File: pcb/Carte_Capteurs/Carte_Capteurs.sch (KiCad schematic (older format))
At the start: 0 parts

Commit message: demarrage carte capteurs
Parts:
- added Logo1: LOGO, Insa:insa-image, symbol insa-sym:LOGO
- added U1: FRDM-KL25Z, Insa:FRDM-KL25Z, symbol Insa:FRDM-KL25Z
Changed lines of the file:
@@
 EESchema Schematic File Version 4
+LIBS:Carte_Capteurs-cache
 EELAYER 26 0
 EELAYER END
@@
 Comment4 ""
 $EndDescr
+$Comp
+L Insa:FRDM-KL25Z U1
+U 1 1 5DFFCA8E
+P 3150 6900
+F 0 "U1" H 3150 9098 50  0000 C CNN
+F 1 "FRDM-KL25Z" H 3150 9007 50  0000 C CNN
+F 2 "Insa:FRDM-KL25Z" H 3100 6250 50  0001 C CNN
+F 3 "" H 3100 6250 50  0001 C CNN
+	1    3150 6900
+	1    0    0    -1
+$EndComp
+$Comp
+L insa-sym:LOGO Logo1
+U 1 1 5DFFCBC5
+P 7550 6800
+F 0 "Logo1" H 7550 6348 60  0001 C CNN
+F 1 "LOGO" H 7550 7252 60  0001 C CNN
+F 2 "Insa:insa-image" H 7550 6800 50  0001 C CNN
+F 3 "" H 7550 6800 50  0001 C CNN
+	1    7550 6800
+	1    0    0    -1
+$EndComp
 $EndSCHEMATC

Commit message: version d'echange
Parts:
- added C1, C4: 100nF, Capacitor_SMD:C_1206_3216Metric_Pad1.42x1.75mm_HandSolder, symbol Device:C
- added C2, C3: 100µF, Capacitor_THT:CP_Radial_D6.3mm_P2.50mm, symbol Device:CP
- added D1: LED, LED_THT:LED_D3.0mm, symbol Device:LED
- added J10, J9: Conn_01x05, Connector_PinHeader_2.54mm:PinHeader_1x05_P2.54mm_Horizontal, symbol Connector_Generic:Conn_01x05
- added J11, J12: Conn_01x04, Connector_PinHeader_2.54mm:PinHeader_1x04_P2.54mm_Horizontal, symbol Connector_Generic:Conn_01x04
- added J5: Conn_02x07_Odd_Even, Connector_PinHeader_2.54mm:PinHeader_2x07_P2.54mm_Vertical, symbol Connector_Generic:Conn_02x07_Odd_Even
- added J6: Molex KK 254, Connector_Molex:Molex_KK-254_AE-6410-04A_1x04_P2.54mm_Vertical, symbol Connector_Generic:Conn_01x04
- added J7, J8: Samtec FTS-105-01-L-DV, Connector_PinHeader_1.27mm:PinHeader_2x05_P1.27mm_Vertical, symbol Connector_Generic:Conn_02x05_Odd_Even
- added R1: R, Resistor_SMD:R_1206_3216Metric_Pad1.42x1.75mm_HandSolder, symbol Device:R
- added U2: XBee, Insa:Xbee3, symbol Insa:XBee
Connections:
- net +BATT: now reaches U1.3.16 (VIN)
- net +BATT: now also C3.1, C4.1, J6.1 (Pin_1)
- net PWR_LED: now reaches U1.3.4 (3V3)
- net PWR_LED: now also D1.2 (A)
- new net: D1.1 (K), R1.1
- new net +3V3: C1.1, C2.1, J6.3 (Pin_3), U2.1 (VCC)
- new net DISABLE_MOT_R: J5.1 (Pin_1)
- new net DISBALE_MOT_L: J5.3 (Pin_3)
- new net FEEDBACK_MOT_L: J5.6 (Pin_6)
- new net FEEDBACK_MOT_R: J5.4 (Pin_4)
- new net GND: C1.2, C2.2, C3.2, C4.2, J5.11 (Pin_11), J5.13 (Pin_13), J5.5 (Pin_5), J5.7 (Pin_7), J5.9 (Pin_9), J6.2 (Pin_2), J6.4 (Pin_4), R1.2, U2.10 (GND)
- new net PWM_MOT_L_1: J5.12 (Pin_12)
- new net PWM_MOT_L_2: J5.14 (Pin_14)
- new net PWM_MOT_R_1: J5.8 (Pin_8)
- new net PWM_MOT_R_2: J5.10 (Pin_10)
- new net SERVO_PWM: J5.2 (Pin_2)
- new net USART_RX: U2.2 (DOUT)
- new net USART_TX: U2.3 (DIN)

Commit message: sauvegarde intermediaire
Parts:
- added C10, C11, C5, C6, C7, C8, C9: 100nF, Capacitor_SMD:C_1206_3216Metric_Pad1.42x1.75mm_HandSolder, symbol Device:C
- added J13: Conn_01x02, Connector_PinHeader_2.54mm:PinHeader_1x02_P2.54mm_Vertical, symbol Connector_Generic:Conn_01x02
- added Q1: NTR3C21NZT1G, Package_TO_SOT_SMD:SOT-23, symbol Device:Q_NMOS_GSD
- added R3, R4: 10K, Resistor_SMD:R_1206_3216Metric_Pad1.42x1.75mm_HandSolder, symbol Device:R
- added R5: 100R, Resistor_SMD:R_1206_3216Metric_Pad1.42x1.75mm_HandSolder, symbol Device:R
- added RN1, RN2: 100R, Resistor_SMD:R_Array_Convex_4x1206, symbol Device:R_Pack04
- added RN3: 10K, Resistor_SMD:R_Array_Convex_4x1206, symbol Device:R_Pack04
- added SW1: SMR8016C-1, Insa:Nidec_Copal_SMR-8016C, symbol Switch:SW_Coded_SH-7050
- added SW2: Reset, Button_Switch_THT:SW_PUSH_6mm_H4.3mm, symbol Switch:SW_Push
- added SW3: USER1, Button_Switch_THT:SW_PUSH_6mm_H4.3mm, symbol Switch:SW_Push
- added SW4: USER2, Button_Switch_THT:SW_PUSH_6mm_H4.3mm, symbol Switch:SW_Push
- added U3: HDSP-7501, Display_7Segment:HDSP-A151, symbol Display_Character:HDSP-7501
- added U4: TCL6C598, Package_SO:TSSOP-16_4.4x5mm_P0.65mm, symbol Insa:TCL6C598
- J10, J9: value Conn_01x05 -> DF3A-5P-2DS; footprint Connector_PinHeader_2.54mm:PinHeader_1x05_P2.54mm_Horizontal -> Insa:DF3A-5P-2DS
- J11, J12: value Conn_01x04 -> DF3A-4P-2DS; footprint Connector_PinHeader_2.54mm:PinHeader_1x04_P2.54mm_Horizontal -> Insa:DF3A-4P-2DS
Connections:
- net DISBALE_MOT_L is gone; now on net DISABLE_MOT_L: J5.3 (Pin_3)
- net +3V3: now also J10.2 (Pin_2), J11.1 (Pin_1), J12.1 (Pin_1), J7.8 (Pin_8), J8.8 (Pin_8), J9.2 (Pin_2), C10.1, C11.1, C5.1, C6.1, C7.1, C8.1, C9.1, R3.1, R4.1, SW1.C, U3.1 (CA), U3.6 (CA), U4.1 (VCC), U4.7 (~CLR)
- net +BATT: now also J13.1 (Pin_1)
- net DISABLE_MOT_R: now also U1.1.1 (PTC7)
- net FEEDBACK_MOT_L: now also U1.2.17 (PTD6)
- net FEEDBACK_MOT_R: now also U1.2.4 (PTD5)
- net GND: now also J10.5 (Pin_5), J11.3 (Pin_3), J12.3 (Pin_3), J7.1 (Pin_1), J7.10 (Pin_10), J7.3 (Pin_3), J7.5 (Pin_5), J7.7 (Pin_7), J7.9 (Pin_9), J8.1 (Pin_1), J8.10 (Pin_10), J8.3 (Pin_3), J8.5 (Pin_5), J8.7 (Pin_7), J8.9 (Pin_9), J9.5 (Pin_5), U1.2.14 (GND), U1.3.12 (GND), U1.3.14 (GND), C10.2, C11.2, C5.2, C6.2, C7.2, C8.2, C9.2, Q1.2 (S), RN3.1 (R1.1), RN3.2 (R2.1), RN3.3 (R3.1), RN3.4 (R4.1), SW2.1, SW3.1, SW4.1, U4.16 (GND), U4.8 (~G)
- net PWM_MOT_L_1: now also U1.1.14 (PTC8)
- net PWM_MOT_L_2: now also U1.1.16 (PTC9)
- net PWM_MOT_R_1: now also U1.1.10 (PTA4)
- net PWM_MOT_R_2: now also U1.1.12 (PTA5)
- net SERVO_PWM: now also U1.1.8 (PTA12)
- net USART_RX: now also U1.4.7 (PTE23)
- net USART_TX: now also U1.4.5 (PTE22)
- net DISP_SIN: now reaches U1.1.11 (PTC6)
- net DISP_SIN: now also U4.2 (SIN)
- net DISP_LATCH: now reaches U1.1.13 (PTC10)
- net DISP_LATCH: now also U4.10 (RCK)
- net ENC_SIG_B1: now reaches U1.1.2 (PTA1)
- net ENC_SIG_B1: now also J9.4 (Pin_4)
- net DISABLE_MOT_L: now reaches U1.1.3 (PTC0)
- net ENC_SIG_B2: now reaches U1.1.4 (PTA2)
- net ENC_SIG_B2: now also J10.4 (Pin_4)
- net ENC_INDEX1: now reaches U1.1.6 (PTD4)
- net ENC_INDEX1: now also J9.1 (Pin_1)
- net DISP_CLK: now reaches U1.1.9 (PTC5)
- net DISP_CLK: now also U4.15 (SRCK)
- net CAM_LED: now reaches U1.2.1 (PTC12)
- net CAM_LED: now also R5.1
- net SW_USER1: now reaches U1.2.10 (PTD3)
- net SW_USER1: now also R3.2, SW3.2
- net SW_USER2: now reaches U1.2.12 (PTD1)
- net SW_USER2: now also R4.2, SW4.2
- net SENS_SCL1: now reaches U1.2.18 (PTE1)
- net SENS_SCL1: now also J11.4 (Pin_4)
- net ENC_INDEX2: now reaches U1.2.2 (PTA13)
- net ENC_INDEX2: now also J10.1 (Pin_1)
- net SENS_SDA1: now reaches U1.2.20 (PTE0)
- net SENS_SDA1: now also J11.2 (Pin_2)
- net CCD_SI0: now reaches U1.3.1 (PTB8)
- net CCD_SI0: now also J7.4 (Pin_4)
- net ROT_SW_2: now reaches U1.3.11 (PTE3)
- net ROT_SW_2: now also RN3.7 (R2.2), SW1.2
- net ROT_SW_4: now reaches U1.3.13 (PTE4)
- net ROT_SW_4: now also RN3.6 (R3.2), SW1.4
- net ROT_SW_8: now reaches U1.3.15 (PTE5)
- net ROT_SW_8: now also RN3.5 (R4.2), SW1.8
- net CCD_CLK0: now reaches U1.3.3 (PTB9)
- net CCD_CLK0: now also J7.6 (Pin_6)
- net CCD_SI1: now reaches U1.3.5 (PTB10)
- net CCD_SI1: now also J8.4 (Pin_4)
- net RESET: now reaches U1.3.6 (PTA20)
- net RESET: now also SW2.2
- net CCD_CLK1: now reaches U1.3.7 (PTB11)
- net CCD_CLK1: now also J8.6 (Pin_6)
- net ROT_SW_1: now reaches U1.3.9 (PTE2)
- net ROT_SW_1: now also RN3.8 (R1.2), SW1.1
- net CCD_AD0: now reaches U1.4.10 (PTC2)
- net CCD_AD0: now also J7.2 (Pin_2)
- net CCD_AD1: now reaches U1.4.12 (PTC1)
- net CCD_AD1: now also J8.2 (Pin_2)
- net SENS_SCL2: now reaches U1.4.2 (PTB0)
- net SENS_SCL2: now also J12.4 (Pin_4)
- net SENS_SDA2: now reaches U1.4.4 (PTB1)
- net SENS_SDA2: now also J12.2 (Pin_2)
- net ENC_SIG_A1: now reaches U1.4.6 (PTB2)
- net ENC_SIG_A1: now also J9.3 (Pin_3)
- net ENC_SIG_A2: now reaches U1.4.8 (PTB3)
- net ENC_SIG_A2: now also J10.3 (Pin_3)
- new net: RN1.4 (R4.1), U3.10 (A)
- new net: RN2.3 (R3.1), U3.2 (F)
- new net: RN2.2 (R2.1), U3.3 (G)
- new net: RN2.4 (R4.1), U3.4 (E)
- new net: RN1.1 (R1.1), U3.5 (D)
- new net: RN2.1 (R1.1), U3.7 (DP)
- new net: RN1.2 (R2.1), U3.8 (C)
- new net: RN1.3 (R3.1), U3.9 (B)
- new net: RN2.5 (R4.2), U4.11 (DRAIN4)
- new net: RN2.6 (R3.2), U4.12 (DRAIN5)
- new net: RN2.7 (R2.2), U4.13 (DRAIN6)
- new net: RN2.8 (R1.2), U4.14 (DRAIN7)
- new net: RN1.5 (R4.2), U4.3 (DRAIN0)
- new net: RN1.6 (R3.2), U4.4 (DRAIN1)
- new net: RN1.7 (R2.2), U4.5 (DRAIN2)
- new net: RN1.8 (R1.2), U4.6 (DRAIN3)
- new net: J13.2 (Pin_2), Q1.3 (D)
- new net: Q1.1 (G), R5.2
- no-connect marks 0 -> 35
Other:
- note added: "CCD Modules 1 & 2"
- note added: "Camera LED control"
- note added: "Control"
- note added: "Encoders"
- note added: "Inputs and Display"
- note added: "Power Supply"
- note added: "RF Module"
- note added: "ToF Sensors"
- moved on the sheet: J10, J11, J12, J5, J7, J8, J9, U1, U2

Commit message: Cartes terminées
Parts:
- added R6, R7, R8, R9: 4.7K, Resistor_SMD:R_1206_3216Metric_Pad1.42x1.75mm_HandSolder, symbol Device:R
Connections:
- net +3V3: now also R6.2, R7.2, R8.2, R9.2
- net SENS_SCL1: now also R8.1
- net SENS_SCL2: now also R6.1
- net SENS_SDA1: now also R9.1
- net SENS_SDA2: now also R7.1
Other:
- note added: "DNP R8 and R9: Already soldered into FRDM board"
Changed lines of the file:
@@
 Wire Wire Line
 	9750 6200 9750 6250
-$Comp
-L Device:R R5
-U 1 1 5D89E15B
-P 9750 5900
-F 0 "R5" V 9850 5850 50  0000 L CNN
-F 1 "100R" V 9650 5800 50  0000 L CNN
-F 2 "Resistor_SMD:R_1206_3216Metric_Pad1.42x1.75mm_HandSolder" V 9680 5900 50  0001 C CNN
-F 3 "~" H 9750 5900 50  0001 C CNN
-	1    9750 5900
-	0    -1   -1   0
-$EndComp
 Wire Wire Line
 	9600 5900 9300 5900
@@
 	2600 5200 3150 5200
 Wire Wire Line
-	4800 5700 5450 5700
-Wire Wire Line
 	4800 4900 5450 4900
 Wire Wire Line
-	4800 5800 5450 5800
-Wire Wire Line
-	4800 6300 5450 6300
-Wire Wire Line
-	4800 6400 5450 6400
-Wire Wire Line
 	4800 6500 5450 6500
 Wire Wire Line
@@
 Wire Wire Line
 	4800 6800 5450 6800
+Wire Wire Line
+	10450 5900 10450 6100
+Wire Wire Line
+	9350 2100 9350 2800
 $Comp
 L Device:Q_NMOS_GSD Q1
@@
 	0    1    1    0
 $EndComp
-Wire Wire Line
-	10450 5900 10450 6100
-Wire Wire Line
-	9350 2100 9350 2800
+$Comp
+L Device:R R5
+U 1 1 5D89E15B
+P 9750 5900
+F 0 "R5" V 9850 5850 50  0000 L CNN
+F 1 "100R" V 9650 5800 50  0000 L CNN
+F 2 "Resistor_SMD:R_1206_3216Metric_Pad1.42x1.75mm_HandSolder" V 9680 5900 50  0001 C CNN
+F 3 "~" H 9750 5900 50  0001 C CNN
+	1    9750 5900
+	0    -1   -1   0
+$EndComp
+$Comp
+L Device:R R6
+U 1 1 5E3A362A
+P 5600 6150
+F 0 "R6" V 5650 5950 50  0000 L CNN
+F 1 "4.7K" V 5500 6050 50  0000 L CNN
+F 2 "Resistor_SMD:R_1206_3216Metric_Pad1.42x1.75mm_HandSolder" V 5530 6150 50  0001 C CNN
+F 3 "~" H 5600 6150 50  0001 C CNN
+	1    5600 6150
+	-1   0    0    1
+$EndComp
+$Comp
+L Device:R R7
+U 1 1 5E3EB1BD
+P 5850 6150
+F 0 "R7" V 5900 6250 50  0000 L CNN
+F 1 "4.7K" V 5750 6050 50  0000 L CNN
+F 2 "Resistor_SMD:R_1206_3216Metric_Pad1.42x1.75mm_HandSolder" V 5780 6150 50  0001 C CNN
+F 3 "~" H 5850 6150 50  0001 C CNN
+	1    5850 6150
+	-1   0    0    1
+$EndComp
+$Comp
+L Device:R R8
+U 1 1 5E4033F4
+P 5600 5550
+F 0 "R8" V 5650 5350 50  0000 L CNN
+F 1 "4.7K" V 5500 5450 50  0000 L CNN
+F 2 "Resistor_SMD:R_1206_3216Metric_Pad1.42x1.75mm_HandSolder" V 5530 5550 50  0001 C CNN
+F 3 "~" H 5600 5550 50  0001 C CNN
+	1    5600 5550
+	-1   0    0    1
+$EndComp
+$Comp
+L Device:R R9
+U 1 1 5E41B406
+P 5850 5550
+F 0 "R9" V 5900 5650 50  0000 L CNN
+F 1 "4.7K" V 5750 5450 50  0000 L CNN
+F 2 "Resistor_SMD:R_1206_3216Metric_Pad1.42x1.75mm_HandSolder" V 5780 5550 50  0001 C CNN
+F 3 "~" H 5850 5550 50  0001 C CNN
+	1    5850 5550
+	-1   0    0    1
+$EndComp
+Wire Wire Line
+	4800 5700 5600 5700
+Wire Wire Line
+	5850 5800 5850 5700
+Wire Wire Line
+	4800 5800 5850 5800
+Wire Wire Line
+	4800 6300 5600 6300
+Wire Wire Line
+	5850 6400 5850 6300
+Wire Wire Line
+	4800 6400 5850 6400
+Wire Wire Line
+	5600 6000 5700 6000
+Wire Wire Line
+	5600 5400 5700 5400
+$Comp
+L power:+3.3V #PWR0144
+U 1 1 5E4C8143
+P 5700 5400
+F 0 "#PWR0144" H 5700 5250 50  0001 C CNN
+F 1 "+3.3V" H 5850 5500 50  0000 C CNN
+F 2 "" H 5700 5400 50  0001 C CNN
+F 3 "" H 5700 5400 50  0001 C CNN
+	1    5700 5400
+	1    0    0    -1
+$EndComp
+$Comp
+L power:+3.3V #PWR0145
+U 1 1 5E4E0D8E
+P 5700 6000
+F 0 "#PWR0145" H 5700 5850 50  0001 C CNN
+F 1 "+3.3V" H 5850 6100 50  0000 C CNN
+F 2 "" H 5700 6000 50  0001 C CNN
+F 3 "" H 5700 6000 50  0001 C CNN
+	1    5700 6000
+	1    0    0    -1
+$EndComp
+Connection ~ 5700 6000
+Wire Wire Line
+	5700 6000 5850 6000
+Connection ~ 5700 5400
+Wire Wire Line
+	5700 5400 5850 5400
+Text Notes 3950 7650 0    50   ~ 0
+DNP R8 and R9: Already soldered into FRDM board
 $EndSCHEMATC

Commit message: Correction sur carte capteur + realisation des pieces du circuit sous LibreCad/InkScape
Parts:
- RN1, RN2: value 100R -> 220R; footprint Resistor_SMD:R_Array_Convex_4x1206 -> Resistor_SMD:R_Array_Convex_4x0603
- RN3: footprint Resistor_SMD:R_Array_Convex_4x1206 -> Resistor_SMD:R_Array_Convex_4x0603
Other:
- note added: "TODO: Rajouter une mesure de VBAT sur une entrée ADC"
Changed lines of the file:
@@
 Sheet 1 1
 Title "Carte_Capteurs"
-Date "2019-07-31"
-Rev "1.0"
+Date "2019-10-09"
+Rev "1.1"
 Comp "INSA Toulouse (GEI)"
 Comment1 ""
@@
 F 0 "RN3" H 7938 3046 50  0000 L CNN
 F 1 "10K" H 7938 2955 50  0000 L CNN
-F 2 "Resistor_SMD:R_Array_Convex_4x1206" V 8025 3000 50  0001 C CNN
+F 2 "Resistor_SMD:R_Array_Convex_4x0603" V 8025 3000 50  0001 C CNN
 F 3 "~" H 7750 3000 50  0001 C CNN
 	1    7750 3000
@@
 P 5350 2500
 F 0 "RN1" V 5675 2500 50  0000 C CNN
-F 1 "100R" V 5584 2500 50  0000 C CNN
-F 2 "Resistor_SMD:R_Array_Convex_4x1206" V 5625 2500 50  0001 C CNN
+F 1 "220R" V 5584 2500 50  0000 C CNN
+F 2 "Resistor_SMD:R_Array_Convex_4x0603" V 5625 2500 50  0001 C CNN
 F 3 "~" H 5350 2500 50  0001 C CNN
 	1    5350 2500
@@
 P 5350 3000
 F 0 "RN2" V 5050 3000 50  0000 C CNN
-F 1 "100R" V 4950 3000 50  0000 C CNN
-F 2 "Resistor_SMD:R_Array_Convex_4x1206" V 5625 3000 50  0001 C CNN
+F 1 "220R" V 4950 3000 50  0000 C CNN
+F 2 "Resistor_SMD:R_Array_Convex_4x0603" V 5625 3000 50  0001 C CNN
 F 3 "~" H 5350 3000 50  0001 C CNN
 	1    5350 3000
@@
 Text Notes 3950 7650 0    50   ~ 0
 DNP R8 and R9: Already soldered into FRDM board
+Text Notes 850  4200 0    50   ~ 0
+TODO: Rajouter une mesure de VBAT sur une entrée ADC
 $EndSCHEMATC

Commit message: correction sur carte capteur
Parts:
- added R10: 4.7K, Resistor_SMD:R_1206_3216Metric_Pad1.42x1.75mm_HandSolder, symbol Device:R
- added R11: 2.2K, Resistor_SMD:R_1206_3216Metric_Pad1.42x1.75mm_HandSolder, symbol Device:R
- R1: value R -> 100R
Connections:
- net +BATT: now also R10.1
- net DISABLE_MOT_L: now also J5.1 (Pin_1); no longer J5.3 (Pin_3)
- net DISABLE_MOT_R: now also J5.3 (Pin_3); no longer J5.1 (Pin_1)
- net FEEDBACK_MOT_L: now also J5.4 (Pin_4); no longer J5.6 (Pin_6)
- net FEEDBACK_MOT_R: now also J5.10 (Pin_10); no longer J5.4 (Pin_4)
- net GND: now also R11.2
- net PWM_MOT_L_1: now also J5.6 (Pin_6); no longer J5.12 (Pin_12)
- net PWM_MOT_L_2: now also J5.8 (Pin_8); no longer J5.14 (Pin_14)
- net PWM_MOT_R_1: now also J5.12 (Pin_12); no longer J5.8 (Pin_8)
- net PWM_MOT_R_2: now also J5.14 (Pin_14); no longer J5.10 (Pin_10)
- net USART_RX: now also U1.4.3 (PTE21); no longer U1.4.7 (PTE23)
- net USART_TX: now also U1.4.1 (PTE20); no longer U1.4.5 (PTE22)
- new net VBAT_ADC: R10.2, R11.1, U1.4.5 (PTE22)
- no-connect marks 35 -> 34
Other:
- note added: "ENC_INDEX_1 ->PTD4 (INT)\nENC_INDEX_2 ->PTA13(INT)\nCCD_AD0 ->ADC0_SE11\nCCD_AD1 ->ADC0_SE15"
- note added: "FEEDBACK_L ->ADC_SE6\nFEEDBACK_R ->ADC_SE7\nENC_SIG_A1 ->FTM2_CH0\nENC_SIG_A2 ->FTM2_CH1"
- note added: "SERVO_PWM ->FTM1_CH0\nPWM_MOT_Rx ->FTM0_CH1 et CH2\nPWM_MOT_Lx ->FTM0_CH4 et CH5"
- note added: "SW_USER1 et 2 -> PTD1 et PTD3 (INT)\nENC_SIG_B1 et B2 -> PTA1 et PTA2 (INT)\nDISP_CLK et DISP_SIN ->SPI0 \n\n"
- note added: "VBAT_ADC->ADC0_SE3\nUART->UART0 (PTE20 et PTE21)\nSENS2 I2C ->I2C0\nSENS1 I2C ->I2C1"
- note removed: "TODO: Rajouter une mesure de VBAT sur une entrée ADC"
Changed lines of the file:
@@
 P 5150 1200
 F 0 "R1" H 5220 1246 50  0000 L CNN
-F 1 "R" H 5220 1155 50  0000 L CNN
+F 1 "100R" H 5220 1155 50  0000 L CNN
 F 2 "Resistor_SMD:R_1206_3216Metric_Pad1.42x1.75mm_HandSolder" V 5080 1200 50  0001 C CNN
 F 3 "~" H 5150 1200 50  0001 C CNN
@@
 	1    0    0    -1
 $EndComp
+Text Label 950  2550 0    50   ~ 0
+DISABLE_MOT_R
+Wire Wire Line
+	950  2550 1550 2550
+Wire Wire Line
+	950  2450 1550 2450
 Text Label 950  2450 0    50   ~ 0
-DISABLE_MOT_R
-Wire Wire Line
-	950  2450 1550 2450
-Wire Wire Line
-	950  2550 1550 2550
-Text Label 950  2550 0    50   ~ 0
 DISABLE_MOT_L
 Text Label 2750 2450 2    50   ~ 0
 SERVO_PWM
+Text Label 2750 2850 2    50   ~ 0
+FEEDBACK_MOT_R
+Wire Wire Line
+	2050 2450 2750 2450
+Wire Wire Line
+	2050 2850 2750 2850
+Wire Wire Line
+	2050 2550 2750 2550
+Wire Wire Line
+	2050 2950 2750 2950
+Wire Wire Line
+	2050 3050 2750 3050
+Wire Wire Line
+	2050 2650 2750 2650
+Wire Wire Line
+	2050 2750 2750 2750
 Text Label 2750 2550 2    50   ~ 0
-FEEDBACK_MOT_R
-Wire Wire Line
-	2050 2450 2750 2450
-Wire Wire Line
-	2050 2550 2750 2550
-Wire Wire Line
-	2050 2650 2750 2650
-Wire Wire Line
-	2050 2750 2750 2750
-Wire Wire Line
-	2050 2850 2750 2850
-Wire Wire Line
-	2050 2950 2750 2950
-Wire Wire Line
-	2050 3050 2750 3050
+FEEDBACK_MOT_L
+Text Label 2750 2950 2    50   ~ 0
+PWM_MOT_R_1
+Text Label 2750 3050 2    50   ~ 0
+PWM_MOT_R_2
 Text Label 2750 2650 2    50   ~ 0
-FEEDBACK_MOT_L
+PWM_MOT_L_1
 Text Label 2750 2750 2    50   ~ 0
-PWM_MOT_R_1
-Text Label 2750 2850 2    50   ~ 0
-PWM_MOT_R_2
-Text Label 2750 2950 2    50   ~ 0
-PWM_MOT_L_1
-Text Label 2750 3050 2    50   ~ 0
 PWM_MOT_L_2
 Text Label 3050 6400 2    50   ~ 0
@@
 	2600 5600 3150 5600
 Wire Wire Line
-	3700 6500 3200 6500
-Wire Wire Line
-	3700 6600 3200 6600
-Text Label 3200 6500 0    50   ~ 0
+	3700 6400 3200 6400
+Wire Wire Line
+	3700 6300 3200 6300
+Text Label 3200 6300 0    50   ~ 0
 USART_TX
-Text Label 3200 6600 0    50   ~ 0
+Text Label 3200 6400 0    50   ~ 0
 USART_RX
 Text Label 5450 6700 2    50   ~ 0
@@
 NoConn ~ 3700 5500
 NoConn ~ 3700 5800
-NoConn ~ 3700 6300
-NoConn ~ 3700 6400
+NoConn ~ 3700 6600
 NoConn ~ 3700 6700
 NoConn ~ 3700 6800
@@
 Text Notes 3950 7650 0    50   ~ 0
 DNP R8 and R9: Already soldered into FRDM board
-Text Notes 850  4200 0    50   ~ 0
-TODO: Rajouter une mesure de VBAT sur une entrée ADC
+Text Notes 700  4300 0    50   ~ 0
+VBAT_ADC->ADC0_SE3\nUART->UART0 (PTE20 et PTE21)\nSENS2 I2C ->I2C0\nSENS1 I2C ->I2C1
+$Comp
+L Device:R R10
+U 1 1 5DB8E05D
+P 6150 7000
+F 0 "R10" H 6220 7046 50  0000 L CNN
+F 1 "4.7K" H 6220 6955 50  0000 L CNN
+F 2 "Resistor_SMD:R_1206_3216Metric_Pad1.42x1.75mm_HandSolder" V 6080 7000 50  0001 C CNN
+F 3 "~" H 6150 7000 50  0001 C CNN
+	1    6150 7000
+	1    0    0    -1
+$EndComp
+$Comp
+L Device:R R11
+U 1 1 5DBA7271
+P 6150 7400
+F 0 "R11" H 6220 7446 50  0000 L CNN
+F 1 "2.2K" H 6220 7355 50  0000 L CNN
+F 2 "Resistor_SMD:R_1206_3216Metric_Pad1.42x1.75mm_HandSolder" V 6080 7400 50  0001 C CNN
+F 3 "~" H 6150 7400 50  0001 C CNN
+	1    6150 7400
+	1    0    0    -1
+$EndComp
+$Comp
+L power:+BATT #PWR0146
+U 1 1 5DBD9FAA
+P 6150 6800
+F 0 "#PWR0146" H 6150 6650 50  0001 C CNN
+F 1 "+BATT" H 6165 6973 50  0000 C CNN
+F 2 "" H 6150 6800 50  0001 C CNN
+F 3 "" H 6150 6800 50  0001 C CNN
+	1    6150 6800
+	1    0    0    -1
+$EndComp
+$Comp
+L power:GND #PWR0147
+U 1 1 5DC25B77
+P 6150 7550
+F 0 "#PWR0147" H 6150 7300 50  0001 C CNN
+F 1 "GND" H 6155 7377 50  0000 C CNN
+F 2 "" H 6150 7550 50  0001 C CNN
+F 3 "" H 6150 7550 50  0001 C CNN
+	1    6150 7550
+	1    0    0    -1
+$EndComp
+Wire Wire Line
+	6150 6800 6150 6850
+Wire Wire Line
+	6150 7150 6150 7200
+Wire Wire Line
+	6150 7200 6850 7200
+Connection ~ 6150 7200
+Wire Wire Line
+	6150 7200 6150 7250
+Wire Wire Line
+	3700 6500 3200 6500
+Text Label 3200 6500 0    50   ~ 0
+VBAT_ADC
+Text Label 6850 7200 2    50   ~ 0
+VBAT_ADC
+Text Notes 2100 4300 0    50   ~ 0
+FEEDBACK_L ->ADC_SE6\nFEEDBACK_R ->ADC_SE7\nENC_SIG_A1 ->FTM2_CH0\nENC_SIG_A2 ->FTM2_CH1
+Text Notes 3200 4200 0    50   ~ 0
+SERVO_PWM ->FTM1_CH0\nPWM_MOT_Rx ->FTM0_CH1 et CH2\nPWM_MOT_Lx ->FTM0_CH4 et CH5
+Text Notes 4700 4300 0    50   ~ 0
+ENC_INDEX_1 ->PTD4 (INT)\nENC_INDEX_2 ->PTA13(INT)\nCCD_AD0 ->ADC0_SE11\nCCD_AD1 ->ADC0_SE15
+Text Notes 700  4650 0    50   ~ 0
+SW_USER1 et 2 -> PTD1 et PTD3 (INT)\nENC_SIG_B1 et B2 -> PTA1 et PTA2 (INT)\nDISP_CLK et DISP_SIN ->SPI0 \n\n
 $EndSCHEMATC

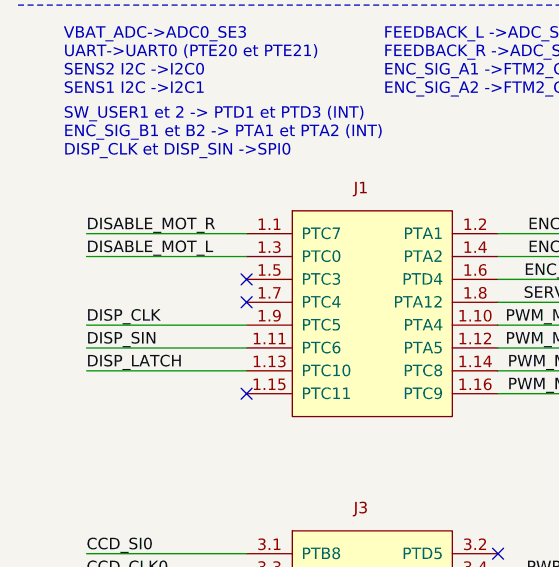
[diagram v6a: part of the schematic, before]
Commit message: creation d'une carte camera et d'une carte pour els led
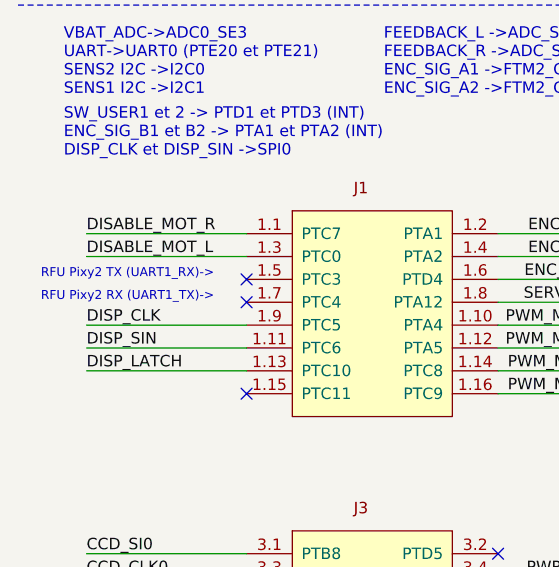
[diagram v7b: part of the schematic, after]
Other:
- note added: "RFU Pixy2 RX (UART1_TX)->"
- note added: "RFU Pixy2 TX (UART1_RX)->"
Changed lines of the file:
@@
 EESchema Schematic File Version 4
-LIBS:Carte_Capteurs-cache
 EELAYER 30 0
 EELAYER END
@@
 Text Notes 700  4650 0    50   ~ 0
 SW_USER1 et 2 -> PTD1 et PTD3 (INT)\nENC_SIG_B1 et B2 -> PTA1 et PTA2 (INT)\nDISP_CLK et DISP_SIN ->SPI0 \n\n
+Text Notes 600  5100 0    39   ~ 0
+RFU Pixy2 TX (UART1_RX)->
+Text Notes 600  5200 0    39   ~ 0
+RFU Pixy2 RX (UART1_TX)->
 $EndSCHEMATC
